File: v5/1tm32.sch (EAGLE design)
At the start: 44 parts, among them IC1 STM32L412RBT6P, J1 DST310S_32.768KHZ, J2 10118192-0001LF, U2 LD39050PU33R, Y1 8MHz

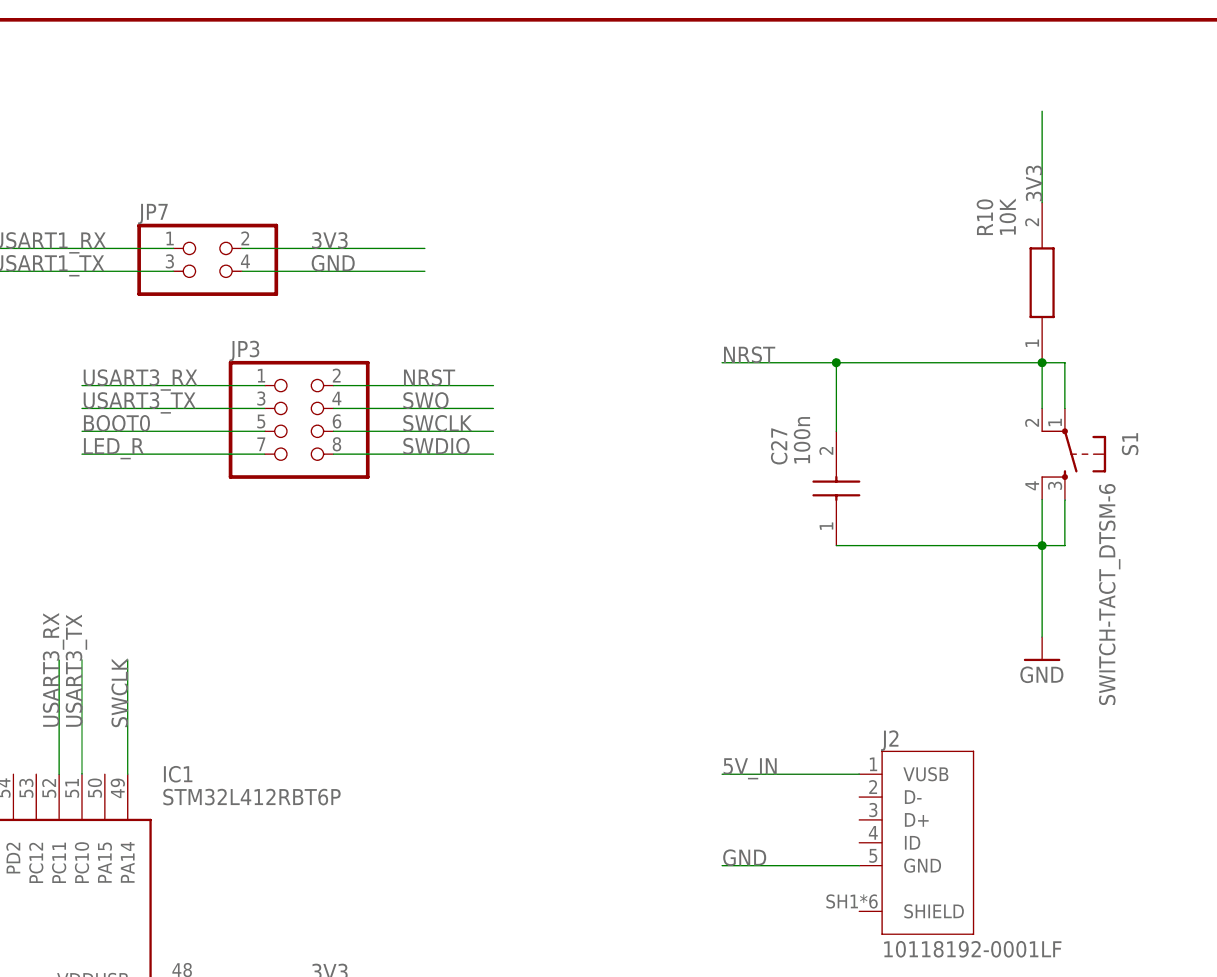
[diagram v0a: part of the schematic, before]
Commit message: removed resistor for switch
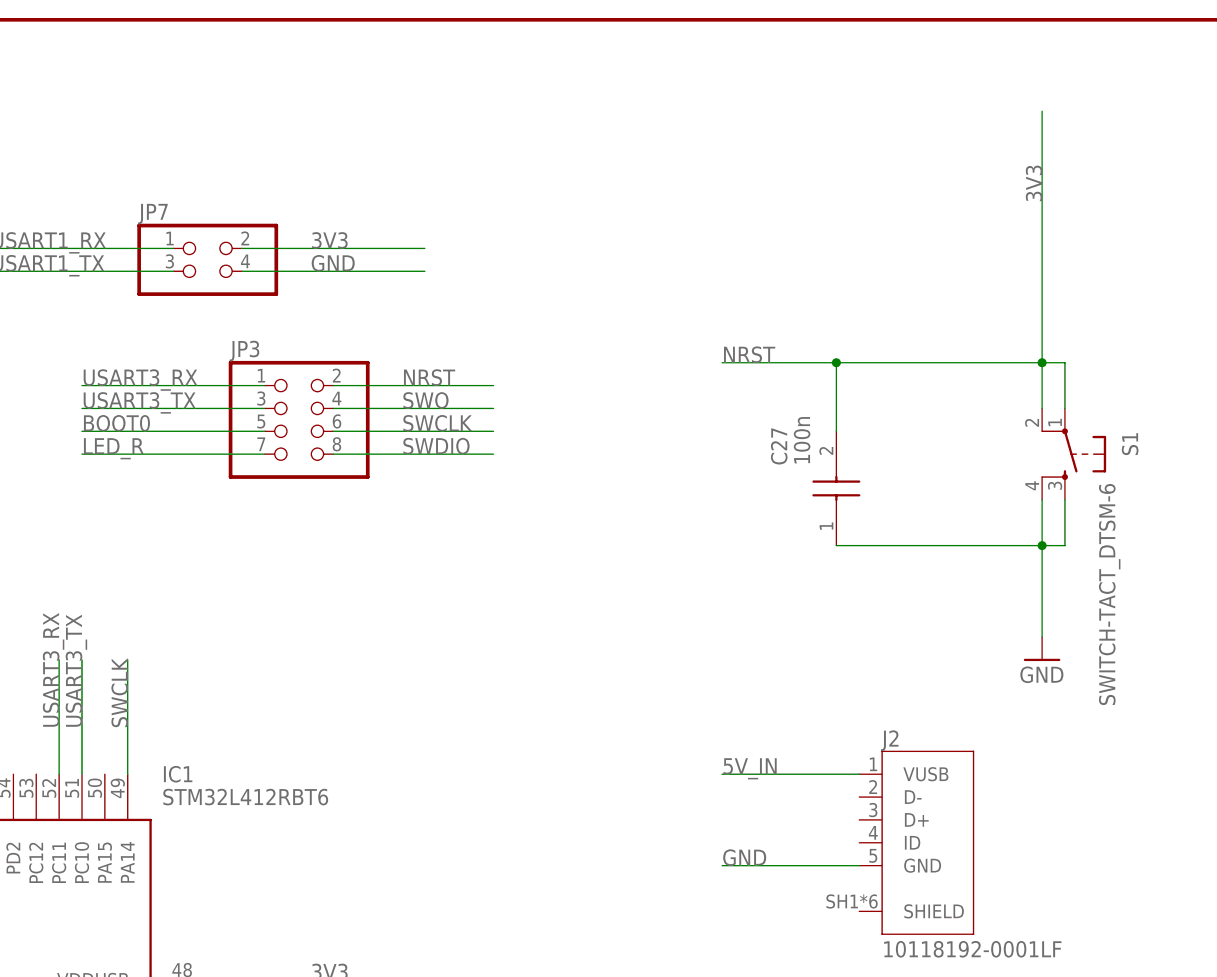
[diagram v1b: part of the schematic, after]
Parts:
- removed R10: 10K, RC0805JR-0710KL:RC0805JR-0710KL
- IC1: value STM32L412RBT6P -> STM32L412RBT6
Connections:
- net 3V3: no longer R10.2
- net NRST: no longer R10.1
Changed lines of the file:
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@@
 <part name="J2" library="ce-capstone" deviceset="10118192-0001LF" device=""/>
 <part name="FRAME1" library="frames" library_urn="urn:adsk.eagle:library:229" deviceset="TABL_L" device=""/>
-<part name="IC1" library="STM32L412RBT6P" deviceset="STM32L412RBT6P" device=""/>
+<part name="IC1" library="STM32L412RBT6P" deviceset="STM32L412RBT6P" device="" value="STM32L412RBT6"/>
 <part name="C1" library="GRM219R61H105KA73D(1u)" deviceset="GRM219R61H105KA73D" device="" value="1u"/>
 <part name="C12" library="GRM219R61H105KA73D(1u)" deviceset="GRM219R61H105KA73D" device="" value="1u"/>
@@
 <part name="R6" library="RC0805FR-131KL" deviceset="RC0805FR-131KL" device="" value="1K"/>
 <part name="R7" library="RC0805FR-131KL" deviceset="RC0805FR-131KL" device="" value="1K"/>
-<part name="R10" library="RC0805JR-0710KL" deviceset="RC0805JR-0710KL" device="" value="10K"/>
 <part name="R1" library="RC0805FR-131KL" deviceset="RC0805FR-131KL" device="" value="1K"/>
 <part name="U$3" library="ce-capstone" deviceset="SML-P12VTT86" device="" value="LED_R"/>
@@
 <attribute name="NAME" x="26.67" y="107.95" size="1.778" layer="95" rot="R90" align="center-left"/>
 <attribute name="VALUE" x="29.21" y="107.95" size="1.778" layer="96" rot="R90" align="center-left"/>
-</instance>
-<instance part="R10" gate="G$1" x="162.56" y="116.84" smashed="yes" rot="R90">
-<attribute name="NAME" x="156.21" y="130.81" size="1.778" layer="95" rot="R90" align="center-left"/>
-<attribute name="VALUE" x="158.75" y="130.81" size="1.778" layer="96" rot="R90" align="center-left"/>
 </instance>
 <instance part="R1" gate="G$1" x="73.66" y="-7.62" smashed="yes" rot="R90">
@@
 </segment>
 <segment>
-<wire x1="162.56" y1="134.62" x2="162.56" y2="144.78" width="0.1524" layer="91"/>
 <label x="162.56" y="134.62" size="1.778" layer="95" rot="R90"/>
-<pinref part="R10" gate="G$1" pin="2"/>
+<wire x1="162.56" y1="144.78" x2="162.56" y2="116.84" width="0.1524" layer="91"/>
 </segment>
 <segment>
@@
 <pinref part="C27" gate="G$1" pin="2"/>
 <wire x1="139.7" y1="116.84" x2="139.7" y2="109.22" width="0.1524" layer="91"/>
-<pinref part="R10" gate="G$1" pin="1"/>
 <pinref part="S1" gate="G$1" pin="2"/>
 <wire x1="162.56" y1="116.84" x2="162.56" y2="111.76" width="0.1524" layer="91"/>
